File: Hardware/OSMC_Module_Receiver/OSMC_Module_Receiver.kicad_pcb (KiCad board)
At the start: 2 copper layers, 39 x 32 mm, 5 parts, among them J1 Conn_01x04_Socket, J2 Conn_01x04_Socket, J3 Conn_01x04_Socket, J4 Conn_01x04_Socket, J5 Conn_01x06_Pin

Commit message: update
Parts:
- J1, J2, J3, J4: footprint Connector_PinSocket_2.54mm:PinSocket_1x04_P2.54mm_Vertical -> Connector_PinHeader_2.54mm:PinHeader_1x04_P2.54mm_Vertical
- J5: footprint Connector_PinHeader_2.54mm:PinHeader_1x06_P2.54mm_Horizontal -> Connector_PinHeader_2.54mm:PinHeader_1x06_P2.54mm_Vertical
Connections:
- net Net-(J4-Pin_1) renamed /IO1
- net Net-(J4-Pin_2) renamed /IO2
- net Net-(J4-Pin_3) renamed /I03
- net Net-(J4-Pin_4) renamed /IO4
- J1 pad 1: Net-(J1-Pin_1) -> /Gnd
- J1 pad 2: Net-(J1-Pin_2) -> /Vdd
- J1 pad 3: unconnected-(J1-Pin_3-Pad3) -> /Vdd
- J1 pad 4: unconnected-(J1-Pin_4-Pad4) -> /Gnd
- J5 pad 1: Net-(J1-Pin_1) -> /Gnd
- J5 pad 2: Net-(J1-Pin_2) -> /Vdd
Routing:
- net /Vdd: track 0.00 -> 41.5 mm
- net Net-(J1-Pin_1): track 35.5 -> 0.00 mm
- net Net-(J1-Pin_2): track 33.4 -> 0.00 mm
- net /IO1: track 21.1 -> 22.0 mm
- added copper zone on B.Cu, net /Gnd
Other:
- board text added: "Receiver V1 10/25"
- board text added: "TO MC"
- board text added: "Up"

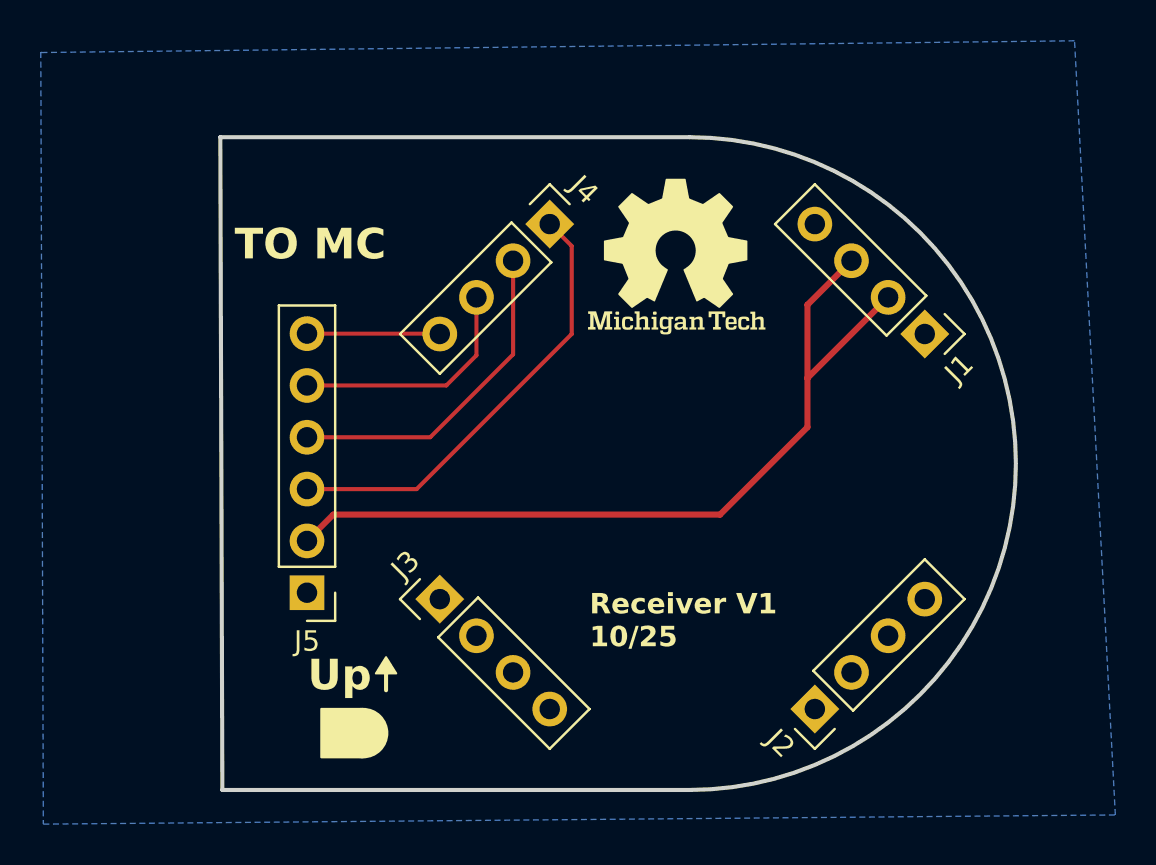
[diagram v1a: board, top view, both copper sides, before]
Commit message: added mounting holes
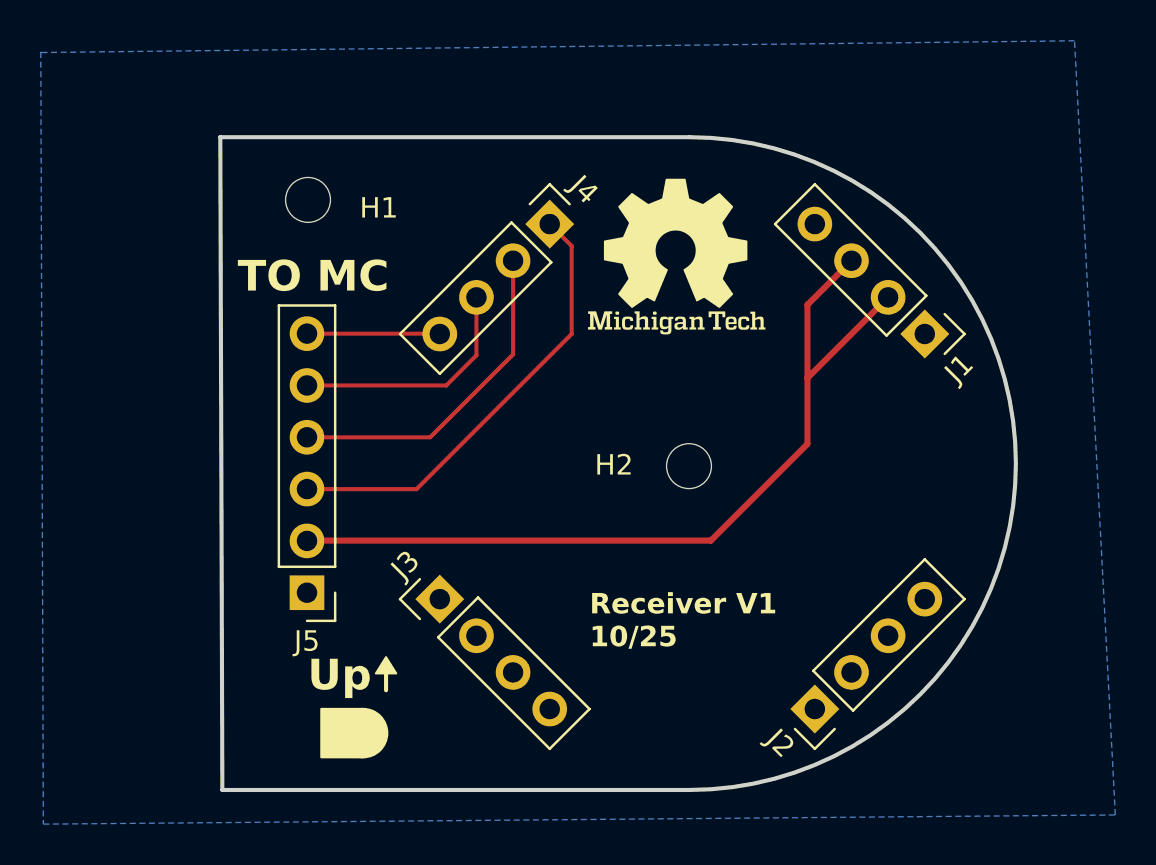
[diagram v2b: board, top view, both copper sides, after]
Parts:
- added H1: MountingHole, MountingHole:MountingHole_2.2mm_M2, F.Cu at (139.3, 48.1)
- added H2: MountingHole, MountingHole:MountingHole_2.2mm_M2, F.Cu at (158.0, 61.1)
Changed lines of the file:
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@@
 	(net 13 "/IO4")
 	(net 14 "/IO1")
+	(footprint "MountingHole:MountingHole_2.2mm_M2"
+		(layer "F.Cu")
+		(at 139.3 48.075)
+		(descr "Mounting Hole 2.2mm, M2, no annular, generated by kicad-footprint-generator mountinghole.py")
+		(tags "mountinghole M2")
+		(property "Reference" "H1"
+			(at 3.475 0.4 0)
+			(layer "F.SilkS")
+			(effects
+				(font
+					(size 1 1)
+					(thickness 0.15)
+				)
+			)
+		)
+		(property "Value" "MountingHole"
+			(at 0 3.15 0)
+			(layer "F.Fab")
+			(effects
+				(font
+					(size 1 1)
+					(thickness 0.15)
+				)
+			)
+		)
+		(property "Datasheet" "~"
+			(at 0 0 0)
+			(layer "F.Fab")
+			(hide yes)
+			(effects
+				(font
+					(size 1.27 1.27)
+					(thickness 0.15)
+				)
+			)
+		)
+		(property "Description" "Mounting Hole without connection"
+			(at 0 0 0)
+			(layer "F.Fab")
+			(hide yes)
+			(effects
+				(font
+					(size 1.27 1.27)
+					(thickness 0.15)
+				)
+			)
+		)
+		(property ki_fp_filters "MountingHole*")
+		(sheetname "/")
+		(sheetfile "OSMC_Module_Receiver.kicad_sch")
+		(attr exclude_from_pos_files exclude_from_bom)
+		(fp_circle
+			(center 0 0)
+			(end 2.2 0)
+			(stroke
+				(width 0.15)
+				(type solid)
+			)
+			(fill no)
+			(layer "Cmts.User")
+		)
+		(fp_circle
+			(center 0 0)
+			(end 2.45 0)
+			(stroke
+				(width 0.05)
+				(type solid)
+			)
+			(fill no)
+			(layer "F.CrtYd")
+		)
+		(fp_text user "${REFERENCE}"
+			(at 0 0 0)
+			(layer "F.Fab")
+			(effects
+				(font
+					(size 1 1)
+					(thickness 0.15)
+				)
+			)
+		)
+		(pad "" np_thru_hole circle
+			(at 0 0)
+			(size 2.2 2.2)
+			(drill 2.2)
+			(layers "*.Cu" "*.Mask")
+		)
+		(embedded_fonts no)
+	)
 	(footprint "Connector_PinHeader_2.54mm:PinHeader_1x04_P2.54mm_Vertical"
 		(layer "F.Cu")
@@
 			)
 		)
+	)
+	(footprint "MountingHole:MountingHole_2.2mm_M2"
+		(layer "F.Cu")
+		(at 157.975 61.125)
+		(descr "Mounting Hole 2.2mm, M2, no annular, generated by kicad-footprint-generator mountinghole.py")
+		(tags "mountinghole M2")
+		(property "Reference" "H2"
+			(at -3.675 -0.05 0)
+			(layer "F.SilkS")
+			(effects
+				(font
+					(size 1 1)
+					(thickness 0.15)
+				)
+			)
+		)
+		(property "Value" "MountingHole"
+			(at 0 3.15 0)
+			(layer "F.Fab")
+			(effects
+				(font
+					(size 1 1)
+					(thickness 0.15)
+				)
+			)
+		)
+		(property "Datasheet" "~"
+			(at 0 0 0)
+			(layer "F.Fab")
+			(hide yes)
+			(effects
+				(font
+					(size 1.27 1.27)
+					(thickness 0.15)
+				)
+			)
+		)
+		(property "Description" "Mounting Hole without connection"
+			(at 0 0 0)
+			(layer "F.Fab")
+			(hide yes)
+			(effects
+				(font
+					(size 1.27 1.27)
+					(thickness 0.15)
+				)
+			)
+		)
+		(property ki_fp_filters "MountingHole*")
+		(sheetname "/")
+		(sheetfile "OSMC_Module_Receiver.kicad_sch")
+		(attr exclude_from_pos_files exclude_from_bom)
+		(fp_circle
+			(center 0 0)
+			(end 2.2 0)
+			(stroke
+				(width 0.15)
+				(type solid)
+			)
+			(fill no)
+			(layer "Cmts.User")
+		)
+		(fp_circle
+			(center 0 0)
+			(end 2.45 0)
+			(stroke
+				(width 0.05)
+				(type solid)
+			)
+			(fill no)
+			(layer "F.CrtYd")
+		)
+		(fp_text user "${REFERENCE}"
+			(at 0 0 0)
+			(layer "F.Fab")
+			(effects
+				(font
+					(size 1 1)
+					(thickness 0.15)
+				)
+			)
+		)
+		(pad "" np_thru_hole circle
+			(at 0 0)
+			(size 2.2 2.2)
+			(drill 2.2)
+			(layers "*.Cu" "*.Mask")
+		)
+		(embedded_fonts no)
 	)
 	(gr_poly
@@
 	)
 	(gr_text "TO MC"
-		(at 135.7 51.125 0)
+		(at 135.85 52.7 0)
 		(layer "F.SilkS")
 		(effects
@@
 	)
 	(segment
-		(start 139.25 64.79)
-		(end 140.54 63.5)
+		(start 139.265 64.775)
+		(end 159.05 64.775)
 		(width 0.3)
 		(layer "F.Cu")
@@
 	)
 	(segment
+		(start 139.25 64.79)
+		(end 139.265 64.775)
+		(width 0.3)
+		(layer "F.Cu")
+		(net 10)
+	)
+	(segment
 		(start 163.781973 53.21487)
 		(end 165.94081 51.056033)
@@
 	)
 	(segment
-		(start 140.54 63.5)
-		(end 159.5 63.5)
+		(start 163.781973 60.043027)
+		(end 163.781973 56.806973)
 		(width 0.3)
 		(layer "F.Cu")
@@
 	)
 	(segment
-		(start 159.5 63.5)
-		(end 163.781973 59.218027)
+		(start 159.05 64.775)
+		(end 163.781973 60.043027)
 		(width 0.3)
 		(layer "F.Cu")
-		(net 10)
-	)
-	(segment
-		(start 163.781973 59.218027)
-		(end 163.781973 56.806973)
-		(width 0.3)
-		(layer "F.Cu")

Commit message: refile zones
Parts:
- moved H2 0.15 mm to (158.0, 61.0)
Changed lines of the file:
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@@
 	(footprint "MountingHole:MountingHole_2.2mm_M2"
 		(layer "F.Cu")
-		(at 157.975 61.125)
+		(at 158 60.975)
 		(descr "Mounting Hole 2.2mm, M2, no annular, generated by kicad-footprint-generator mountinghole.py")
 		(tags "mountinghole M2")
